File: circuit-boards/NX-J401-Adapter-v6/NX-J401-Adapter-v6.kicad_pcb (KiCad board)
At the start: 4 copper layers, 120 x 79 mm, 129 parts, among them J1 SWD, J10 NX CONTROL & UART, J12 NX CONTROL & UART, J13 NX CONTROL & UART, J14 USB_C_Receptacle_USB2.0_14P, J2 POWER, J3 USB1, J4 Terminal, J5 CAN1, J6 Terminal, J7 15V, Q10 CSD19534Q5A, Q2 CSD19534Q5A, Q3 CSD19534Q5A, Q4 CSD17578Q5A, Q5 CSD17578Q5A, Q6 SI2301CDS-T1-GE3, Q7 SS8050, Q8 SI2301CDS-T1-GE3, Q9 CSD19534Q5A, SW1 RECOVERY, SW2 RESET, U2 LM74700QDBVRQ1, U3 STM32G431CBTx, U4 TJA1051T/3/1J, U5 TPS613222ADBV, U6 LM74700QDBVRQ1, U8 FT232RNL, U9 ISO6721BDR

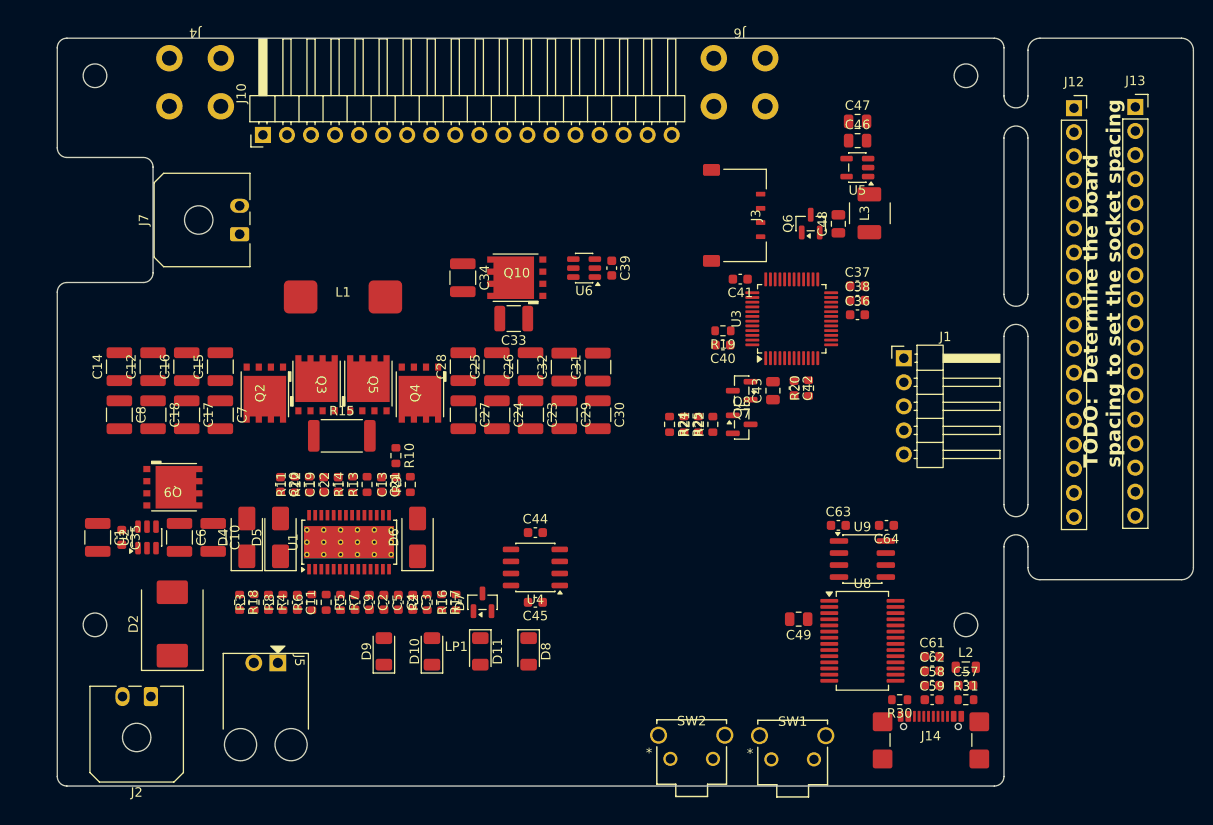
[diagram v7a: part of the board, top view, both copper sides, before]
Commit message: Initial fully routed PCB
Signed-off-by: Scott Berman <sgberman1@gmail.com>
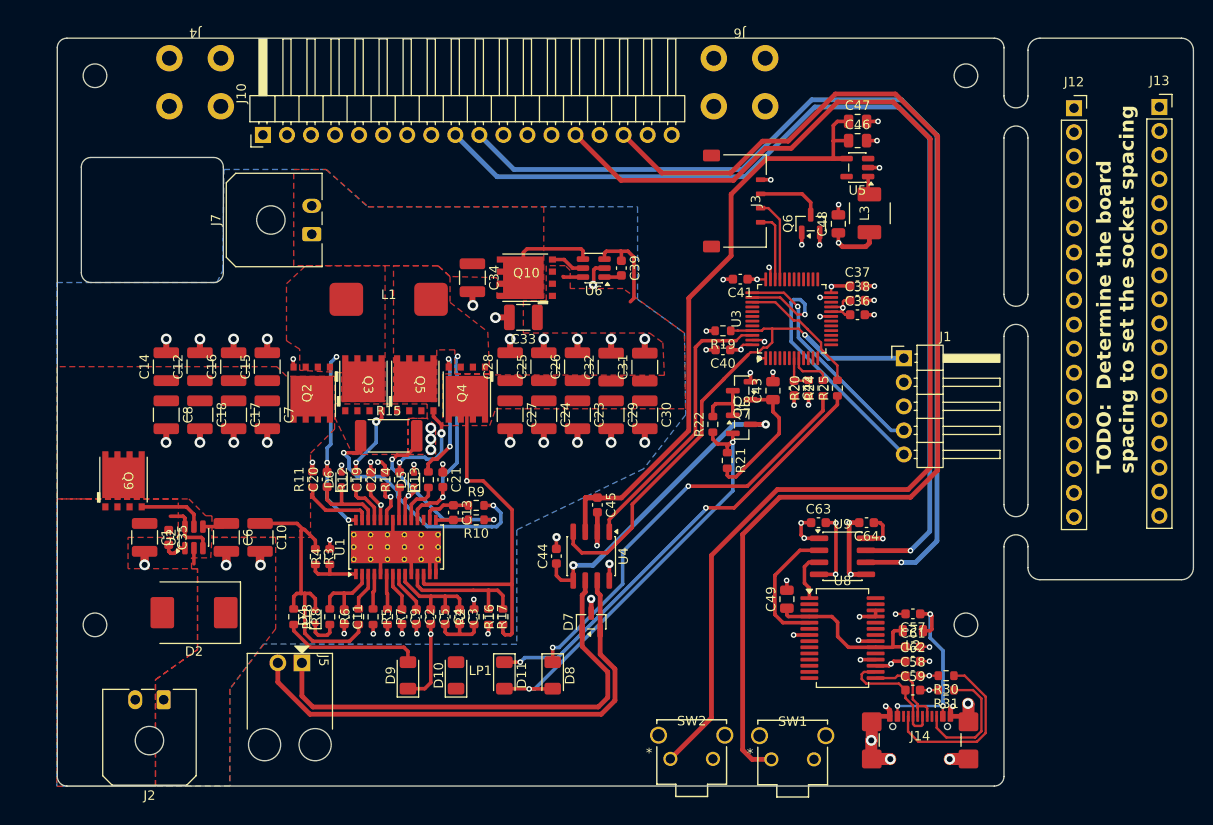
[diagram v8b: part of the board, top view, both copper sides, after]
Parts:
- D4, D5, D6: value B260A-13-F -> BAT54KFILM; footprint Diode_SMD:D_SMA -> Diode_SMD:D_SOD-523
- moved R24 16.7 mm to (236.9, 111.5), turned to 90 degrees
- moved R25 16.7 mm to (238.4, 111.5), turned to 90 degrees
- moved D5 15.4 mm to (193.7, 121.2)
- moved C45 12.2 mm to (213.1, 123.8), turned to -90 degrees
- moved D7 11.7 mm to (212.4, 136.2)
- moved D4 11.1 mm to (183.3, 135.6)
- moved R10 10.9 mm to (200.3, 125.4), turned to 180 degrees
- moved D6 10.1 mm to (186.0, 121.1)
- moved C57 9.39 mm to (246.4, 135.3), turned to 180 degrees
- moved R3 8.08 mm to (183.3, 129.3), turned to -90 degrees
- moved R4 8.08 mm to (184.8, 129.3), turned to 90 degrees
- moved J7 7.62 mm to (182.9, 95.2)
- moved R9 7.30 mm to (200.3, 123.9), turned to 0 degrees
- moved L2 6.79 mm to (246.4, 137.1), turned to 180 degrees
- moved C13 6.76 mm to (197.8, 124.6), turned to -90 degrees
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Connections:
- C20 pad 1: Net-(D5-K) -> Net-(D6-K)
- C21 pad 1: Net-(D6-K) -> Net-(D5-K)
- C64 pad 1: /3V3 -> /3V3_BTN
- D11 pad 1: /CANable2.0/STAT_LED -> Net-(D11-K)
- D11 pad 2: Net-(D11-A) -> /CANable2.0/3V3
- D8 pad 1: /CANable2.0/WORD_LED -> Net-(D8-K)
- D8 pad 2: Net-(D8-A) -> /CANable2.0/3V3
- J10 pad 13: /GND_BTN -> GND1
- J10 pad 15: /GND_BTN -> GND1
- J10 pad 3: /GND_BTN -> GND1
- R24 pad 1: /CANable2.0/3V3 -> Net-(D8-K)
- R24 pad 2: Net-(D8-A) -> /CANable2.0/WORD_LED
- R25 pad 1: /CANable2.0/3V3 -> Net-(D11-K)
- R25 pad 2: Net-(D11-A) -> /CANable2.0/STAT_LED
- U1 pad 12: unconnected-(U1-VOSNS-Pad12) -> /15V 3A Buck-Boost Power Supply/+V_OUT
- U1 pad 20: Net-(D6-K) -> Net-(D5-K)
- U1 pad 26: Net-(D5-K) -> Net-(D6-K)
- U9 pad 8: /3V3 -> /3V3_BTN
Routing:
- net /~{SYS_RESET}: track 0.00 -> 129.4 mm
- net /~{REC}: track 0.00 -> 125.1 mm
- net /UART2_TXD: track 0.00 -> 105.8 mm, vias 0 -> 1
- net /UART2_RXD: track 0.00 -> 105.5 mm, vias 0 -> 1
- net GND: track 0.00 -> 89.4 mm, vias 0 -> 40
- net /15V 3A Buck-Boost Power Supply/+V_OUT: track 0.00 -> 67.2 mm, vias 0 -> 2
- net /CANable2.0/3V3: track 0.00 -> 67.0 mm, vias 0 -> 10
- net /CANable2.0/5V_CAN: track 0.00 -> 66.3 mm
- net /CANable2.0/BOOT0: track 0.00 -> 56.6 mm, vias 0 -> 1
- net /CANable2.0/CAN_H: track 0.00 -> 53.1 mm
- net /CANable2.0/CAN_L: track 0.00 -> 50.3 mm
- net Net-(D11-K): track 0.00 -> 47.5 mm, vias 0 -> 2
- net Net-(D8-K): track 0.00 -> 44.0 mm, vias 0 -> 2
- net GND_USB: track 0.00 -> 40.3 mm, vias 0 -> 18
- net /VIN_PS: track 0.00 -> 33.6 mm
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- added copper zone on F.Cu, net /15V 3A Buck-Boost Power Supply/+V_OUT
- added copper zone on F.Cu, net /15V 3A Buck-Boost Power Supply/RCS
- added copper zone on F.Cu, net /15V 3A Buck-Boost Power Supply/SW1
- added copper zone on F.Cu, net /15V 3A Buck-Boost Power Supply/SW2
- added copper zone on In1.Cu, net /3V3_BTN
- added copper zone on In2.Cu, net /CANable2.0/3V3
- added copper zone on In1.Cu, net /CANable2.0/GND_CAN
- added copper zone on F.Cu, net /VIN_PS
- added copper zone on F.Cu, net /V_IN
- added copper zone on F.Cu, net /V_OUT
- added copper zone on In2.Cu, net 3V3_USB
- added copper zone on B.Cu, net GND
- added copper zone on F.Cu, net GND
- added copper zone on In1.Cu, net GND
- added copper zone on In2.Cu, net GND
- added copper zone on In2.Cu, net GND1
- added copper zone on In1.Cu, net GND_USB
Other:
- outline, holes or cut-outs redrawn
